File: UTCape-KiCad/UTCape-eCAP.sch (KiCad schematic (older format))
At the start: 9 parts, among them IC5 LM555

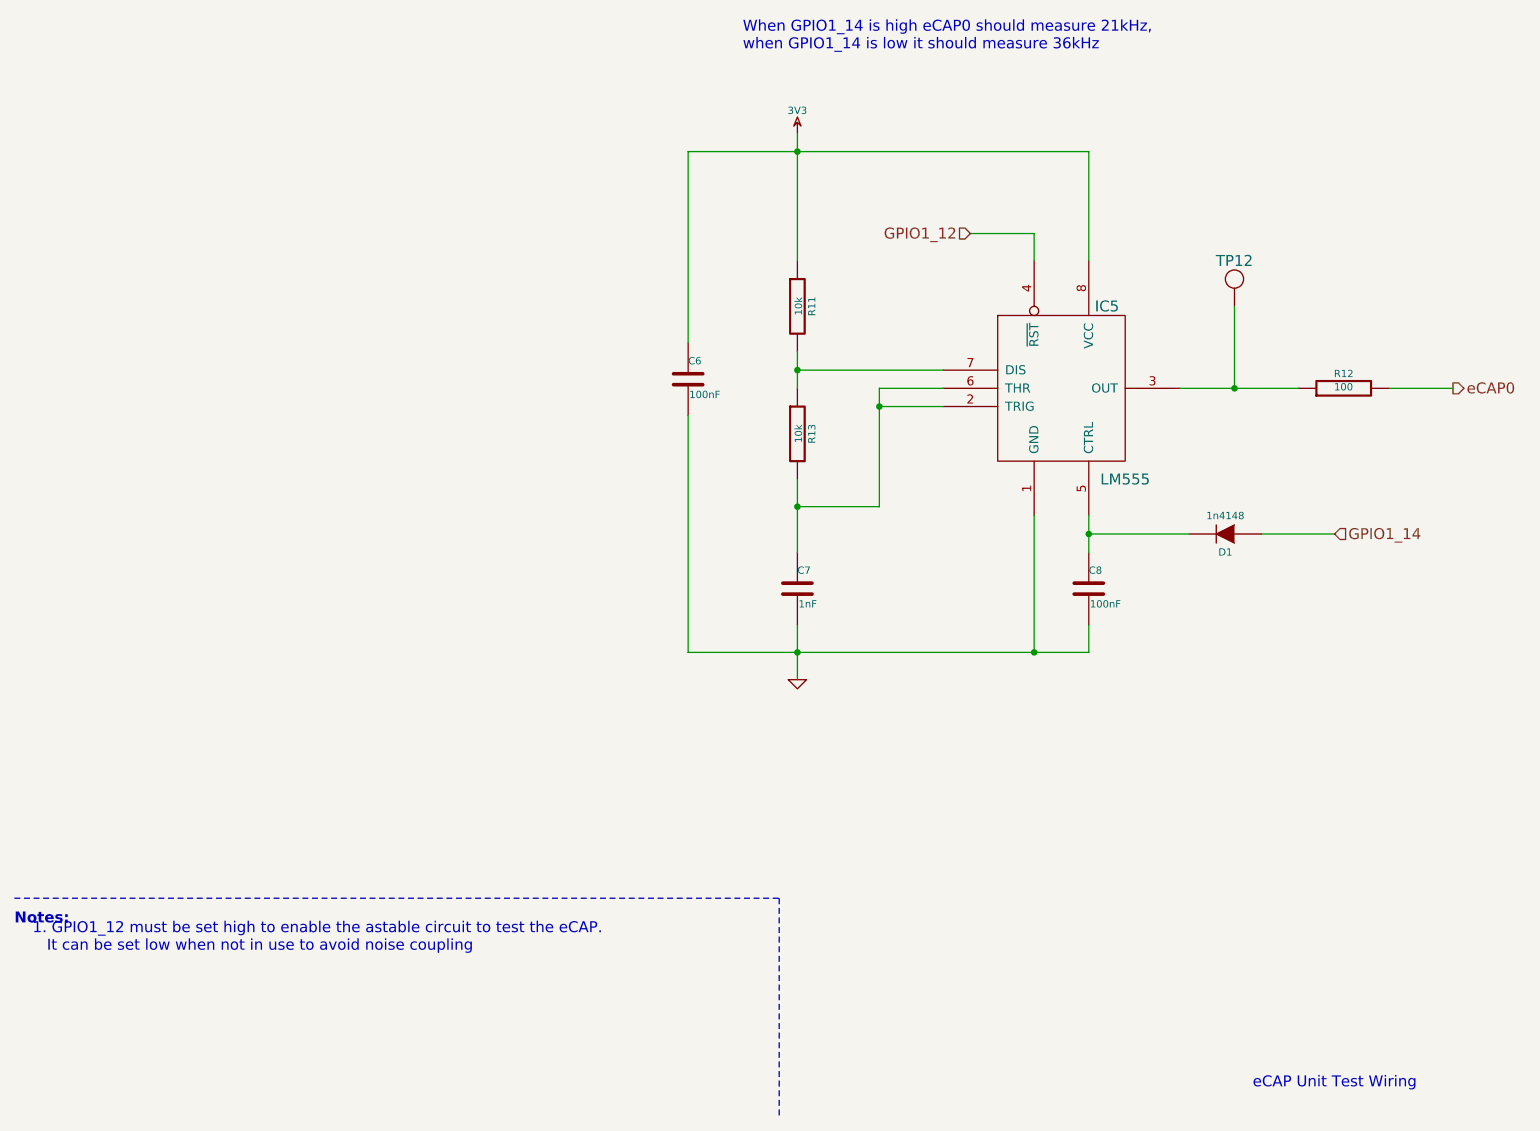
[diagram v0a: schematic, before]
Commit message: layed out PCB, some minor wiring changes for layout
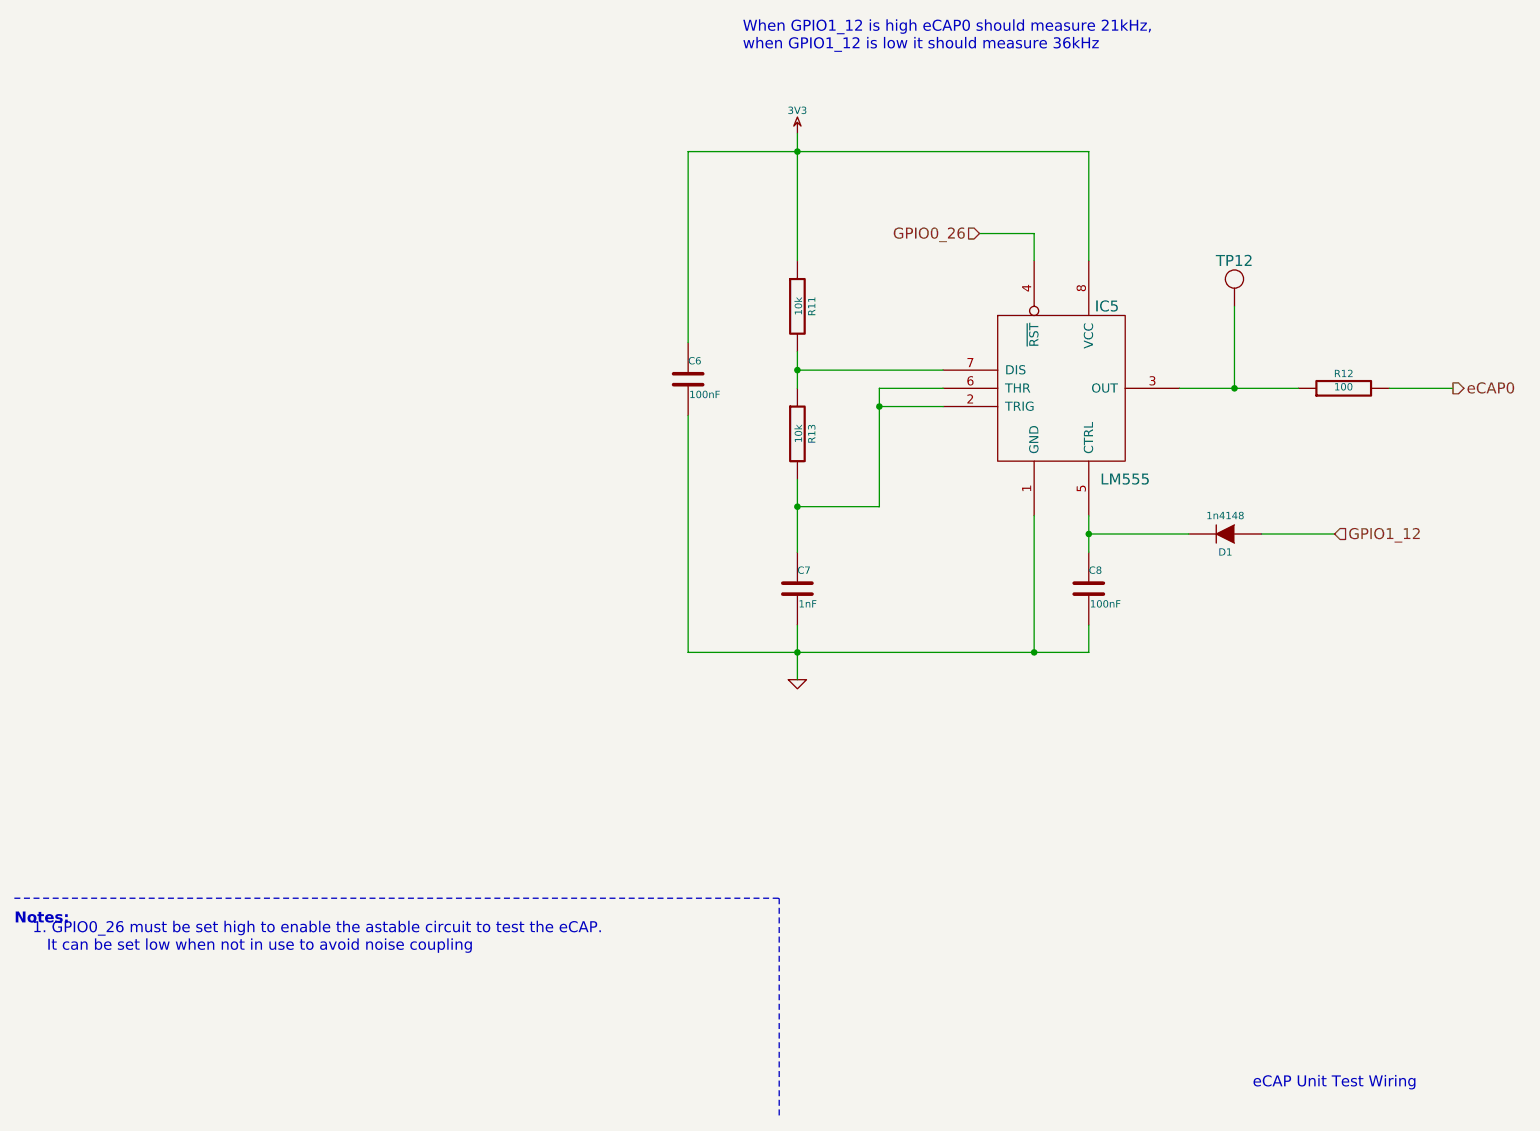
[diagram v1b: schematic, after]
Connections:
- net GPIO1_14 is gone; now on net GPIO1_12: D1.1 (A)
- net GPIO1_12: no longer IC5.4 (~RST)
- new net GPIO0_26: IC5.4 (~RST)
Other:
- note added: "1. GPIO0_26 must be set high to enable the astable circuit to test the eCAP.\n It can be set low when not in use to avoid noise coupling"
- note added: "When GPIO1_12 is high eCAP0 should measure 21kHz, \nwhen GPIO1_12 is low it should measure 36kHz"
- note removed: "1. GPIO1_12 must be set high to enable the astable circuit to test the eCAP.\n It can be set low when not in use to avoid noise coupling"
- note removed: "When GPIO1_14 is high eCAP0 should measure 21kHz, \nwhen GPIO1_14 is low it should measure 36kHz"
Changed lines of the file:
@@
 LIBS:contrib
 LIBS:valves
+LIBS:beagleboneblack
 LIBS:GrayCatLabs
-LIBS:BeagleBoneBlack
 LIBS:UTCape-cache
 EELAYER 27 0
@@
 Text HLabel 8450 3700 2    60   Output ~ 0
 eCAP0
-Text HLabel 5800 2850 0    60   Input ~ 0
+Text HLabel 7800 4500 2    60   Input ~ 0
 GPIO1_12
-Text HLabel 7800 4500 2    60   Input ~ 0
-GPIO1_14
+Text HLabel 5850 2850 0    60   Input ~ 0
+GPIO0_26
 $Comp
 L GND #PWR015
@@
 	4750 6500 4750 7700
 Text Notes 650  6800 0    60   ~ 0
-1. GPIO1_12 must be set high to enable the astable circuit to test the eCAP.\n   It can be set low when not in use to avoid noise coupling
-Wire Wire Line
-	5800 2850 6150 2850
+1. GPIO0_26 must be set high to enable the astable circuit to test the eCAP.\n   It can be set low when not in use to avoid noise coupling
 Text Notes 4550 1850 0    60   ~ 0
-When GPIO1_14 is high eCAP0 should measure 21kHz, \nwhen GPIO1_14 is low it should measure 36kHz
-Wire Wire Line
-	6150 2850 6150 3000
+When GPIO1_12 is high eCAP0 should measure 21kHz, \nwhen GPIO1_12 is low it should measure 36kHz
 Wire Wire Line
 	6450 2400 6450 3000
@@
 	-1   0    0    1
 $EndComp
-Wire Wire Line
-	7800 4500 7400 4500
 Wire Wire Line
 	7000 4500 6450 4500
@@
 03 43 83 61 8C 09 03 03 03 03 43 83 61 8C 09 03 03 03 03 43 83 61 8C 09 03 03 03 03 43 83 61 03
 60 D2 64 32 30 30 30 30 34 84 CF 1C 00 A9 00 9C 01 A8 8B 59 19 06 06 06 06 06 E9 E3 33 80 C5 FF
-07 47 25 A5 D2 E9 03 52 D8 00 00 00 00 49 45 4E 44 AE 42 60 82 76 $EndBitmap
+07 47 25 A5 D2 E9 03 52 D8 00 00 00 00 49 45 4E 44 AE 42 60 82 4A $EndBitmap
 EndData
 $EndBitmap
+Wire Wire Line
+	5850 2850 6150 2850
+Wire Wire Line
+	6150 2850 6150 3000
+Wire Wire Line
+	7400 4500 7800 4500
 $EndSCHEMATC
